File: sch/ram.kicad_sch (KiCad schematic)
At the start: 0 parts

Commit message: Sch:  RAM part w.i.p.
Data path completed, address MUX to be done.
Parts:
- added D18: (no value), symbol 74xx:74LS32
- added D19, D20, D21, D22, D23, D24, D25, D26: 4164, symbol memories:4164
- added D27: 8282, symbol intel8080:8282
- added D51: 74LS153, symbol 74xx:74LS153
- added R30, R38, R40: (no value), symbol Device:R_Small
- added R31, R39: ~, symbol Device:R_Small
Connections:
- new net: D18.8, D27.9 (~{OE})
- new net: D19.15 (~{CAS}), D20.15 (~{CAS}), D21.15 (~{CAS}), D22.15 (~{CAS}), D23.15 (~{CAS}), D24.15 (~{CAS}), D25.15 (~{CAS}), D26.15 (~{CAS}), R39.2
- new net: D19.3 (~{W}), D20.3 (~{W}), D21.3 (~{W}), D22.3 (~{W}), D23.3 (~{W}), D24.3 (~{W}), D25.3 (~{W}), D26.3 (~{W}), R40.2
- new net: D19.4 (~{RAS}), D20.4 (~{RAS}), D21.4 (~{RAS}), D22.4 (~{RAS}), D23.4 (~{RAS}), D24.4 (~{RAS}), D25.4 (~{RAS}), D26.4 (~{RAS}), R38.2
- new net +5V: D19.16 (VCC), D20.16 (VCC), D21.16 (VCC), D22.16 (VCC), D23.16 (VCC), D24.16 (VCC), D25.16 (VCC), D26.16 (VCC), D27.20 (VCC)
- new net 0_ROMSEL: D18.9
- new net A0: D51.4 (I2a)
- new net A1: D51.12 (I2b)
- new net A8: D51.3 (I3a)
- new net A9: D51.13 (I3b)
- new net D0: D19. (DI), D27.12 (B7)
- new net D1: D20. (DI), D27.13 (B6)
- new net D2: D21. (DI), D27.14 (B5)
- new net D3: D22. (DI), D27.15 (B4)
- new net D4: D23. (DI), D27.16 (B3)
- new net D5: D24. (DI), D27.17 (B2)
- new net D6: D25. (DI), D27.18 (B1)
- new net D7: D26. (DI), D27.19 (B0)
- new net GND: D19.8 (GND), D20.8 (GND), D21.8 (GND), D22.8 (GND), D23.8 (GND), D24.8 (GND), D25.8 (GND), D26.8 (GND), D27.10 (GND), D51.1 (Ea), D51.15 (Eb)
- new net K0: D51.14 (S0)
- new net K1: D51.2 (S1)
- new net MA0: D51.7 (Za), R30.1
- new net MA1: D51.9 (Zb), R31.1
- new net RAM_RD_STRB: D27.11 (STB)
- new net RD0: D19.14 (DO), D27.8 (A7)
- new net RD1: D20.14 (DO), D27.7 (A6)
- new net RD2: D21.14 (DO), D27.6 (A5)
- new net RD3: D22.14 (DO), D27.5 (A4)
- new net RD4: D23.14 (DO), D27.4 (A3)
- new net RD5: D24.14 (DO), D27.3 (A2)
- new net RD6: D25.14 (DO), D27.2 (A1)
- new net RD7: D26.14 (DO), D27.1 (A0)
- new net t13: D51.5 (I1a)
- new net t14: D51.11 (I1b)
- new net t4: D51.6 (I0a)
- new net t5: D51.10 (I0b)
- new net xMA0: D19.5 (A0), D20.5 (A0), D21.5 (A0), D22.5 (A0), D23.5 (A0), D24.5 (A0), D25.5 (A0), D26.5 (A0), R30.2
- new net xMA1: D19.7 (A1), D20.7 (A1), D21.7 (A1), D22.7 (A1), D23.7 (A1), D24.7 (A1), D25.7 (A1), D26.7 (A1), R31.2
- new net xMA2: D19.6 (A2), D20.6 (A2), D21.6 (A2), D22.6 (A2), D23.6 (A2), D24.6 (A2), D25.6 (A2), D26.6 (A2)
- new net xMA3: D19.12 (A3), D20.12 (A3), D21.12 (A3), D22.12 (A3), D23.12 (A3), D24.12 (A3), D25.12 (A3), D26.12 (A3)
- new net xMA4: D19.11 (A4), D20.11 (A4), D21.11 (A4), D22.11 (A4), D23.11 (A4), D24.11 (A4), D25.11 (A4), D26.11 (A4)
- new net xMA5: D19.10 (A5), D20.10 (A5), D21.10 (A5), D22.10 (A5), D23.10 (A5), D24.10 (A5), D25.10 (A5), D26.10 (A5)
- new net xMA6: D19.13 (A6), D20.13 (A6), D21.13 (A6), D22.13 (A6), D23.13 (A6), D24.13 (A6), D25.13 (A6), D26.13 (A6)
- new net xMA7: D19.9 (A7), D20.9 (A7), D21.9 (A7), D22.9 (A7), D23.9 (A7), D24.9 (A7), D25.9 (A7), D26.9 (A7)
- new net ~{CAS}: R39.1
- new net ~{MEMR}: D18.10
- new net ~{RAS}: R38.1
- new net ~{WE}: R40.1

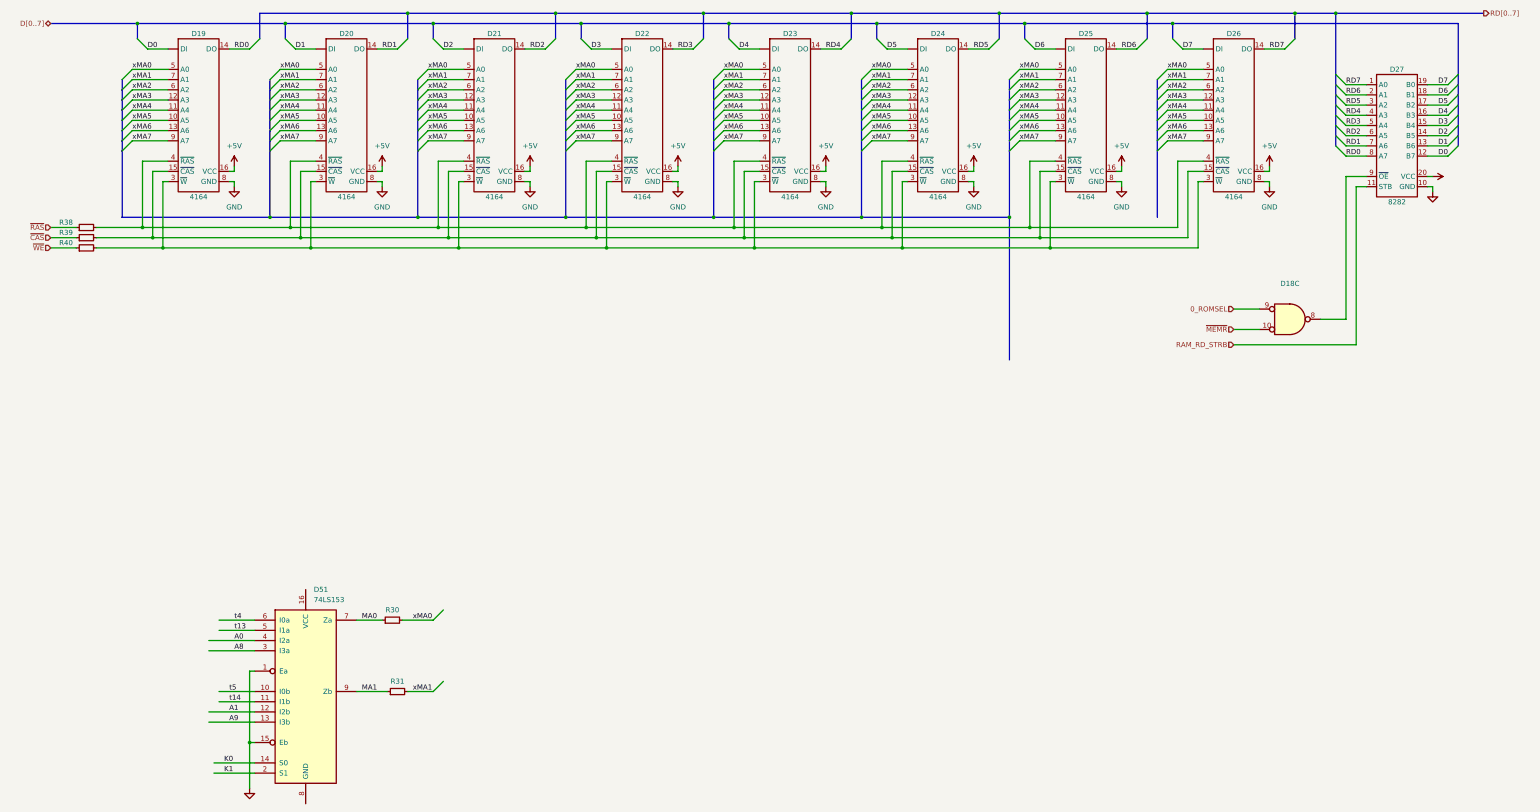
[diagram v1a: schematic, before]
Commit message: Sch:  RAM sheet completed
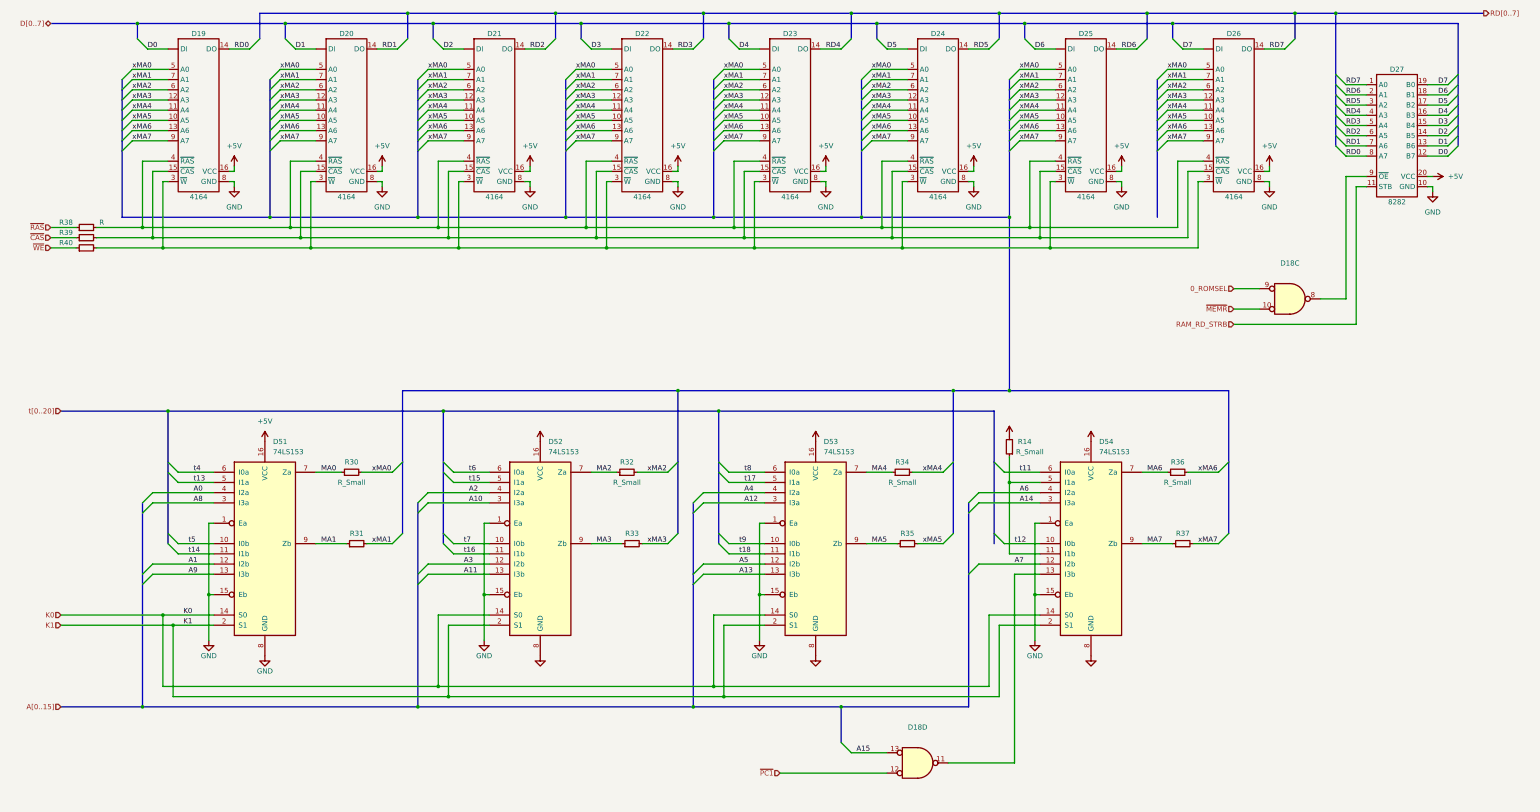
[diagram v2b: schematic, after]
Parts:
- added unit 4 of D18
- added D52, D53, D54: 74LS153, symbol 74xx:74LS153
- added R14, R32, R34, R36: R_Small, symbol Device:R_Small
- added R33, R35, R37: ~, symbol Device:R_Small
- R30: value (none) -> R_Small
- R38: value (none) -> R
- R40: value (none) -> ~
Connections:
- net +5V: now also D51.16 (VCC), D52.16 (VCC), D53.16 (VCC), D54.16 (VCC), R14.2
- net GND: now also D51.8 (GND), D52.1 (Ea), D52.15 (Eb), D52.8 (GND), D53.1 (Ea), D53.15 (Eb), D53.8 (GND), D54.1 (Ea), D54.15 (Eb), D54.8 (GND)
- net K0: now also D52.14 (S0), D53.14 (S0), D54.14 (S0)
- net K1: now also D52.2 (S1), D53.2 (S1), D54.2 (S1)
- net xMA2: now also R32.2
- net xMA3: now also R33.2
- net xMA4: now also R34.2
- net xMA5: now also R35.2
- net xMA6: now also R36.2
- net xMA7: now also R37.2
- new net: D54.11 (I1b), D54.5 (I1a), R14.1
- new net: D18.11, D54.13 (I3b)
- new net A10: D52.3 (I3a)
- new net A11: D52.13 (I3b)
- new net A12: D53.3 (I3a)
- new net A13: D53.13 (I3b)
- new net A14: D54.3 (I3a)
- new net A15: D18.13
- new net A2: D52.4 (I2a)
- new net A3: D52.12 (I2b)
- new net A4: D53.4 (I2a)
- new net A5: D53.12 (I2b)
- new net A6: D54.4 (I2a)
- new net A7: D54.12 (I2b)
- new net MA2: D52.7 (Za), R32.1
- new net MA3: D52.9 (Zb), R33.1
- new net MA4: D53.7 (Za), R34.1
- new net MA5: D53.9 (Zb), R35.1
- new net MA6: D54.7 (Za), R36.1
- new net MA7: D54.9 (Zb), R37.1
- new net t11: D54.6 (I0a)
- new net t12: D54.10 (I0b)
- new net t15: D52.5 (I1a)
- new net t16: D52.11 (I1b)
- new net t17: D53.5 (I1a)
- new net t18: D53.11 (I1b)
- new net t6: D52.6 (I0a)
- new net t7: D52.10 (I0b)
- new net t8: D53.6 (I0a)
- new net t9: D53.10 (I0b)
- new net ~{PC1}: D18.12
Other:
- moved on the sheet: D18C, D51, R30, R31

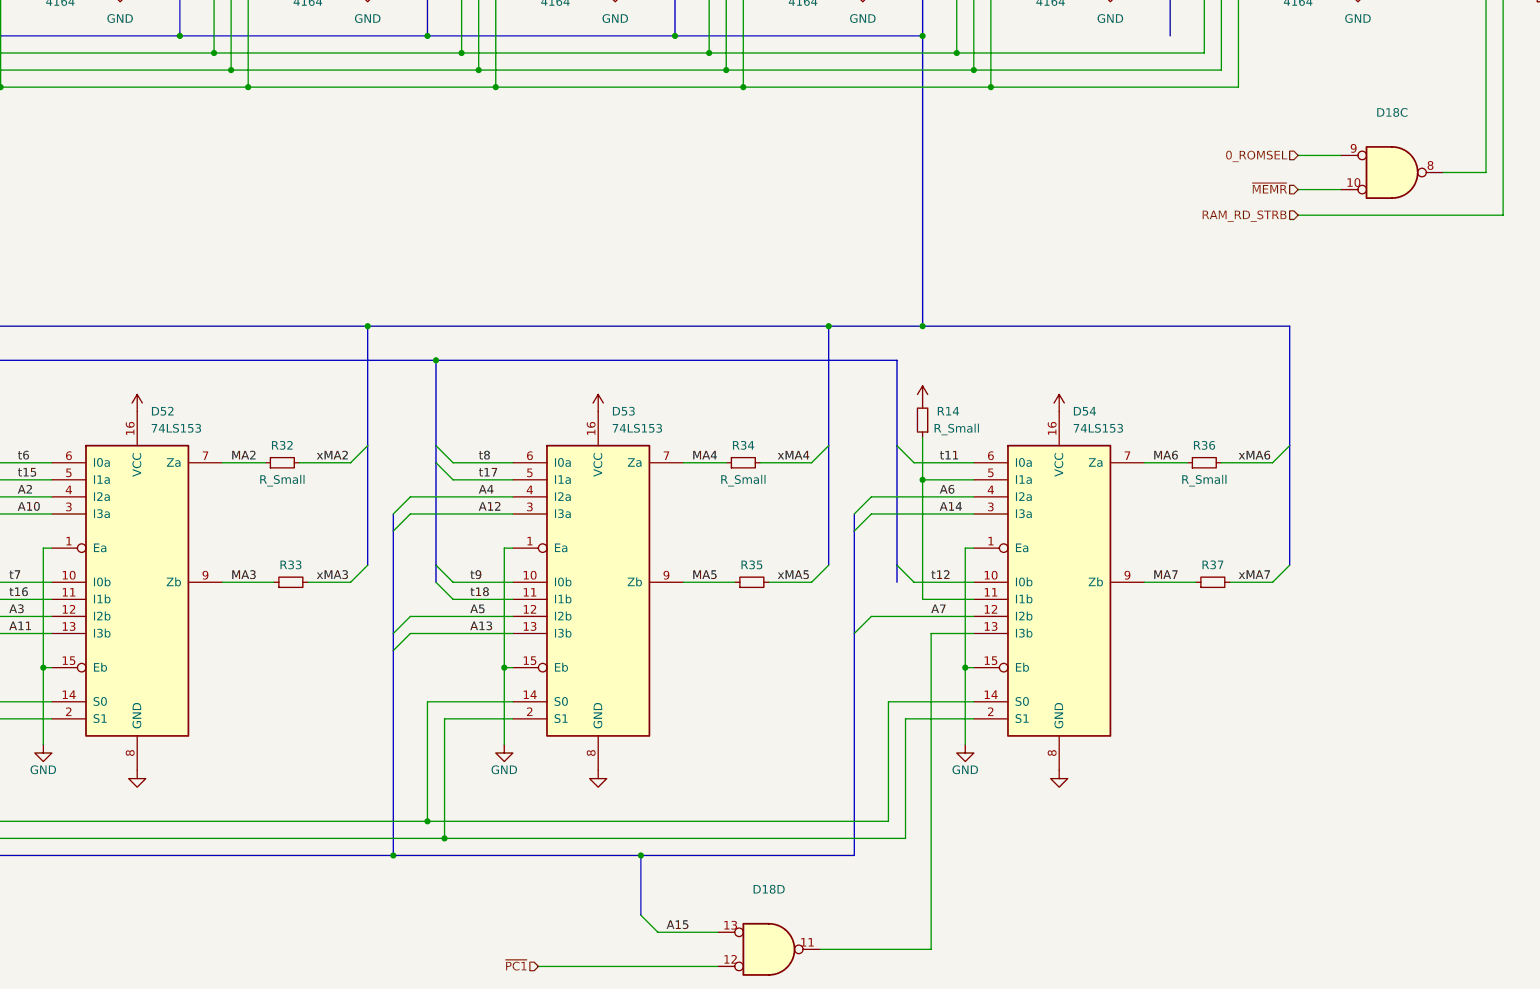
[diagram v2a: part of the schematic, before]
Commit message: Sch: started timing block
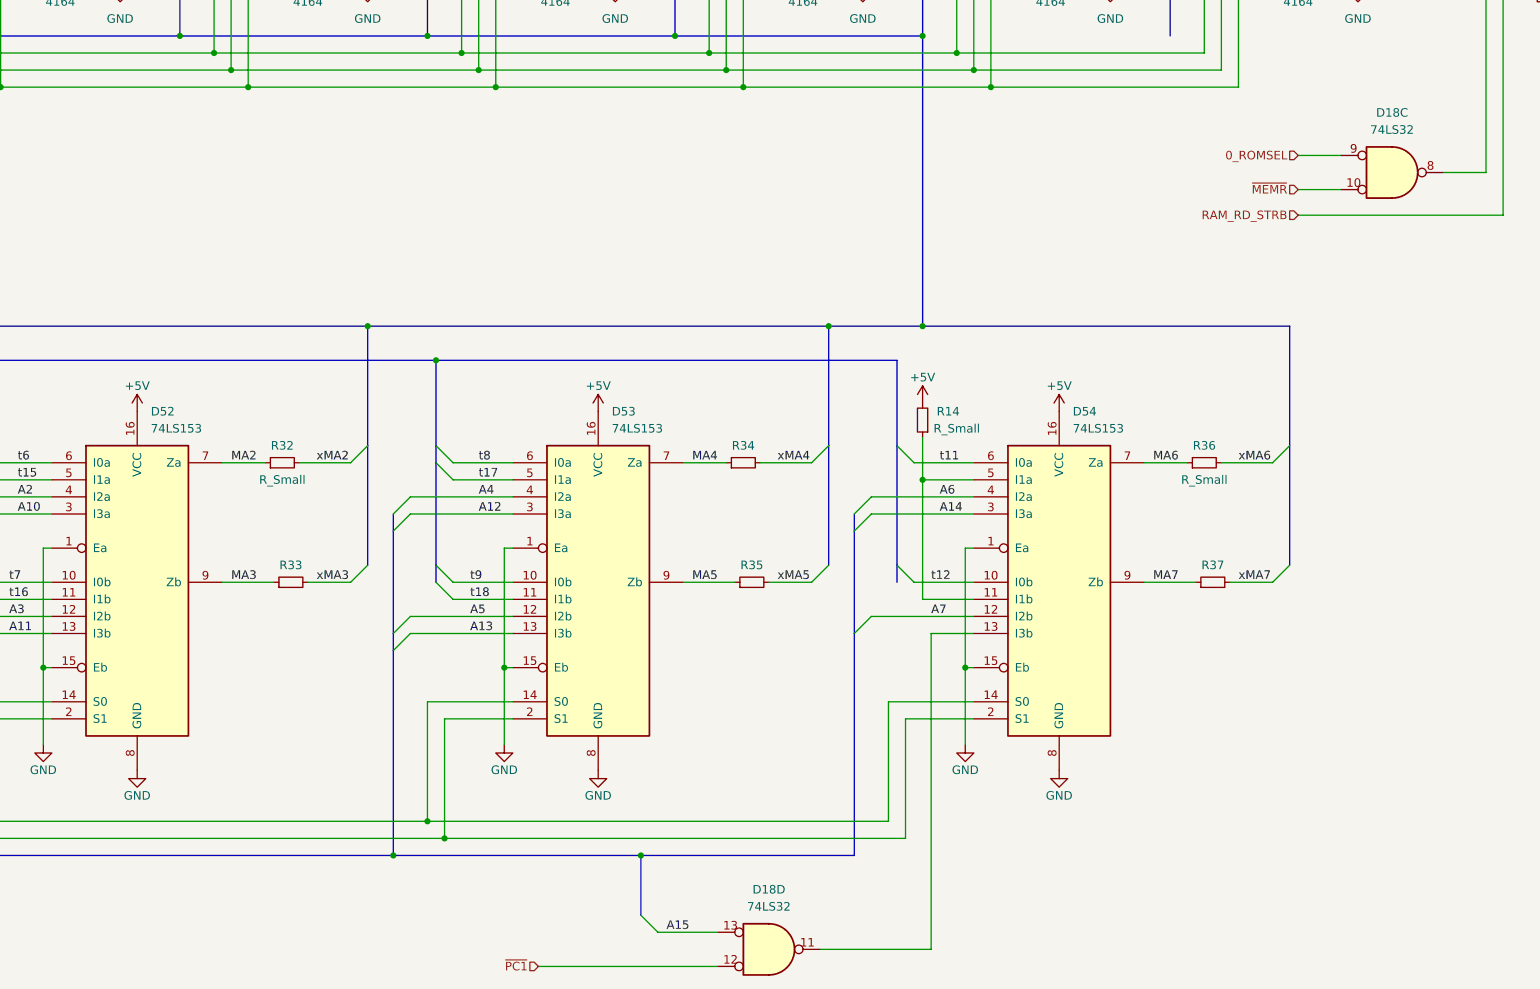
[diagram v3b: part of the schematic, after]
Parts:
- D18: value (none) -> 74LS32
- R34: value R_Small -> (none)
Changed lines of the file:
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@@
     (in_bom yes) (on_board yes) (fields_autoplaced)
     (property "Reference" "D18" (id 0) (at 340.36 87.63 0))
-    (property "Value" "" (id 1) (at 340.36 90.17 0))
+    (property "Value" "74LS32" (id 1) (at 340.36 90.17 0))
     (property "Footprint" "" (id 2) (at 340.36 96.52 0)
       (effects (font (size 1.27 1.27)) hide)
@@
       (effects (font (size 1.27 1.27)) hide)
     )
-    (property "Value" "" (id 1) (at 290.83 128.27 0))
+    (property "Value" "+5V" (id 1) (at 290.83 128.27 0))
     (property "Footprint" "" (id 2) (at 290.83 132.08 0)
       (effects (font (size 1.27 1.27)) hide)
@@
       (effects (font (size 1.27 1.27)) hide)
     )
-    (property "Value" "" (id 1) (at 290.83 189.23 0))
+    (property "Value" "GND" (id 1) (at 290.83 189.23 0))
     (property "Footprint" "" (id 2) (at 290.83 185.42 0)
       (effects (font (size 1.27 1.27)) hide)
@@
       (effects (font (size 1.27 1.27)) hide)
     )
-    (property "Value" "" (id 1) (at 222.25 128.27 0))
+    (property "Value" "+5V" (id 1) (at 222.25 128.27 0))
     (property "Footprint" "" (id 2) (at 222.25 132.08 0)
       (effects (font (size 1.27 1.27)) hide)
@@
       (effects (font (size 1.27 1.27)) hide)
     )
-    (property "Value" "" (id 1) (at 270.51 127 0))
+    (property "Value" "+5V" (id 1) (at 270.51 127 0))
     (property "Footprint" "" (id 2) (at 270.51 130.81 0)
       (effects (font (size 1.27 1.27)) hide)
@@
     (in_bom yes) (on_board yes) (fields_autoplaced)
     (property "Reference" "D18" (id 0) (at 247.65 203.2 0))
-    (property "Value" "" (id 1) (at 247.65 205.74 0))
+    (property "Value" "74LS32" (id 1) (at 247.65 205.74 0))
     (property "Footprint" "" (id 2) (at 247.65 212.09 0)
       (effects (font (size 1.27 1.27)) hide)
@@
       (effects (font (size 1.27 1.27)) hide)
     )
-    (property "Value" "" (id 1) (at 222.25 189.23 0))
+    (property "Value" "GND" (id 1) (at 222.25 189.23 0))
     (property "Footprint" "" (id 2) (at 222.25 185.42 0)
       (effects (font (size 1.27 1.27)) hide)
@@
       (effects (font (size 1.27 1.27)) hide)
     )
-    (property "Value" "" (id 1) (at 153.67 189.23 0))
+    (property "Value" "GND" (id 1) (at 153.67 189.23 0))
     (property "Footprint" "" (id 2) (at 153.67 185.42 0)
       (effects (font (size 1.27 1.27)) hide)
@@
       (effects (font (size 1.27 1.27)) hide)
     )
-    (property "Value" "" (id 1) (at 153.67 128.27 0))
+    (property "Value" "+5V" (id 1) (at 153.67 128.27 0))
     (property "Footprint" "" (id 2) (at 153.67 132.08 0)
       (effects (font (size 1.27 1.27)) hide)
@@
     (in_bom yes) (on_board yes)
     (property "Reference" "R34" (id 0) (at 243.84 137.16 90))
-    (property "Value" "R_Small" (id 1) (at 243.84 142.24 90))
+    (property "Value" "" (id 1) (at 243.84 142.24 90))
     (property "Footprint" "" (id 2) (at 243.84 139.7 0)
       (effects (font (size 1.27 1.27)) hide)

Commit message: Sch: timing sheet - added all elements
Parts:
- R34: value (none) -> R_Small
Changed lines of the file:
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@@
     (in_bom yes) (on_board yes)
     (property "Reference" "R34" (id 0) (at 243.84 137.16 90))
-    (property "Value" "" (id 1) (at 243.84 142.24 90))
+    (property "Value" "R_Small" (id 1) (at 243.84 142.24 90))
     (property "Footprint" "" (id 2) (at 243.84 139.7 0)
       (effects (font (size 1.27 1.27)) hide)

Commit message: SCH: timing block - work in progress
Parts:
- D18: value 74LS32 -> (none)
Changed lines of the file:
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@@
     (in_bom yes) (on_board yes) (fields_autoplaced)
     (property "Reference" "D18" (id 0) (at 340.36 87.63 0))
-    (property "Value" "74LS32" (id 1) (at 340.36 90.17 0))
+    (property "Value" "" (id 1) (at 340.36 90.17 0))
     (property "Footprint" "" (id 2) (at 340.36 96.52 0)
       (effects (font (size 1.27 1.27)) hide)
@@
     (in_bom yes) (on_board yes) (fields_autoplaced)
     (property "Reference" "D18" (id 0) (at 247.65 203.2 0))
-    (property "Value" "74LS32" (id 1) (at 247.65 205.74 0))
+    (property "Value" "" (id 1) (at 247.65 205.74 0))
     (property "Footprint" "" (id 2) (at 247.65 212.09 0)
       (effects (font (size 1.27 1.27)) hide)

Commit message: Extracted RAM controller
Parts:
- D18: value (none) -> 7432
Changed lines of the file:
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@@
     (in_bom yes) (on_board yes) (fields_autoplaced)
     (property "Reference" "D18" (id 0) (at 340.36 87.63 0))
-    (property "Value" "" (id 1) (at 340.36 90.17 0))
+    (property "Value" "7432" (id 1) (at 340.36 90.17 0))
     (property "Footprint" "" (id 2) (at 340.36 96.52 0)
       (effects (font (size 1.27 1.27)) hide)
@@
     (in_bom yes) (on_board yes) (fields_autoplaced)
     (property "Reference" "D18" (id 0) (at 247.65 203.2 0))
-    (property "Value" "" (id 1) (at 247.65 205.74 0))
+    (property "Value" "7432" (id 1) (at 247.65 205.74 0))
     (property "Footprint" "" (id 2) (at 247.65 212.09 0)
       (effects (font (size 1.27 1.27)) hide)

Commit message: Minor renames
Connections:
- net 0_ROMSEL renamed ROM_OE
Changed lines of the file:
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@@
     (effects (font (size 1.27 1.27)) (justify right))
   )
-  (hierarchical_label "0_ROMSEL" (shape input) (at 326.39 93.98 180)
+  (hierarchical_label "ROM_OE" (shape input) (at 326.39 93.98 180)
     (effects (font (size 1.27 1.27)) (justify right))
   )
